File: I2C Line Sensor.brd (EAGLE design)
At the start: 63.5 x 12.1 mm, 31 parts, among them U1 ADS7830

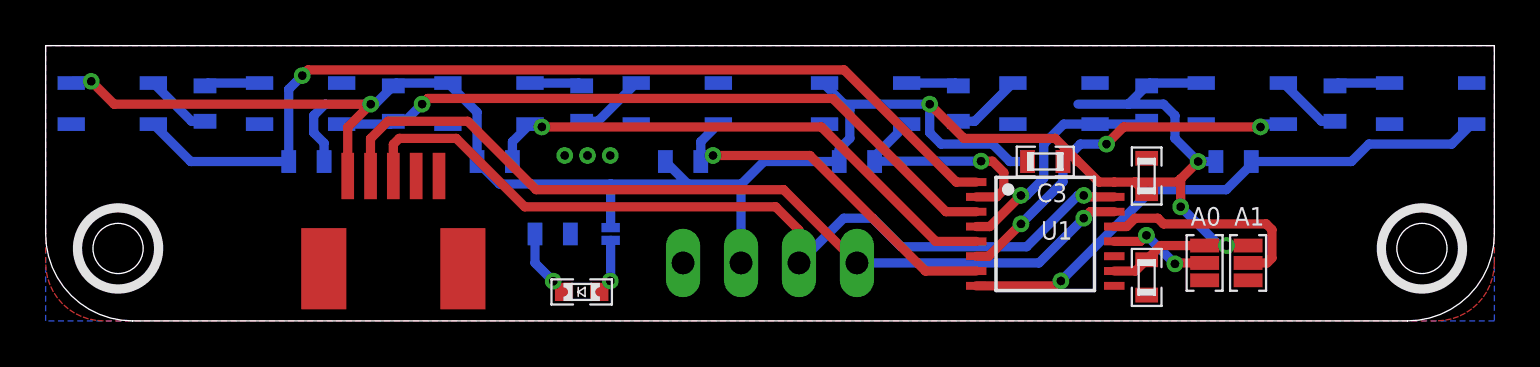
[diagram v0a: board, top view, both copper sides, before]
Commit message: Cleaned up I2C Line Sensor. Added 5 ohm resistor as per datasheet. Updated footprints and removed Zero Force Connector.
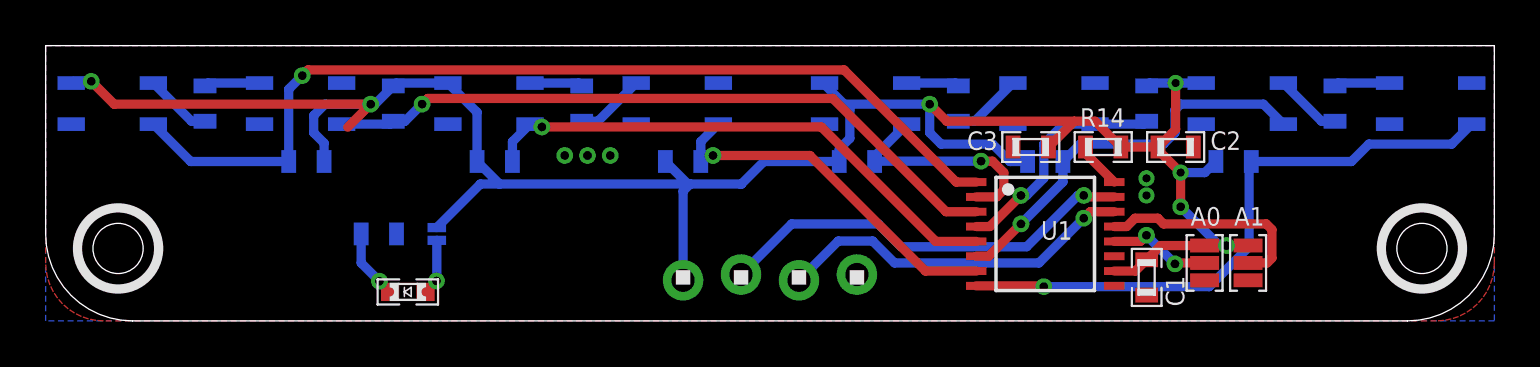
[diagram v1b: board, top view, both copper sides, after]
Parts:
- removed JP1: (no value), microbuilder:1X04_OVAL
- added R14: 5, standardparts:0603
- C1, C2, C3, R1, R10, R11, R12, R13, R2, R3, R4, R5, R6, R7, R8, R9: device .standardparts:0603 -> standardparts:0603
- LED1: device .standardparts:0603.LED -> standardparts:0603.LED
- U$11: value FC1-05-02-T-WT -> 1X4.LOCK; device samtec:FC1-05-02-T-WT -> headers(.1in):1X4.LOCK
- moved U$11 13.5 mm to (27.9, 1.91), turned to 0 degrees
- moved J1 7.62 mm to (17.1, 3.81)
- moved LED1 7.62 mm to (15.9, 1.27)
- moved R13 7.62 mm to (14.6, 3.81)
- moved C2 1.80 mm to (49.5, 7.62), turned to 180 degrees
- moved C3 0.90 mm to (43.2, 7.62)
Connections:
- new net N$15: R14.1, U1.16
- net 3.3V: now also R14.2, U$11.1; no longer JP1.3, U$11.5, U1.16
- net GND: now also U$11.4; no longer JP1.4, U$11.2
- net SCL: now also U$11.3; no longer JP1.1, U$11.4
- net SDA: now also U$11.2; no longer JP1.2, U$11.3
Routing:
- net SCL: track 38.1 -> 15.9 mm
- net SDA: track 38.5 -> 18.7 mm
- net 3.3V: track 103.0 -> 99.3 mm, vias 6 -> 7
- net N$15: track 0.00 -> 2.06 mm
- net H: track 24.8 -> 26.8 mm
- net G: track 16.4 -> 17.7 mm, vias 3 -> 1
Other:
- board text added: "AnomalousMaker.com"
- board text added: "Cruz Monrreal II"
- board text added: "I2C Line Sensor"
- board text removed: "PWR"
